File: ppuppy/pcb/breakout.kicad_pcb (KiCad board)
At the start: 2 copper layers, 48 parts, among them Q1 2N3904, Q2 2N3904, Q3 2N3904, Q4 2N3904, Q5 2N3904, Q6 2N3904, Q7 2N3904, Q8 2N3904

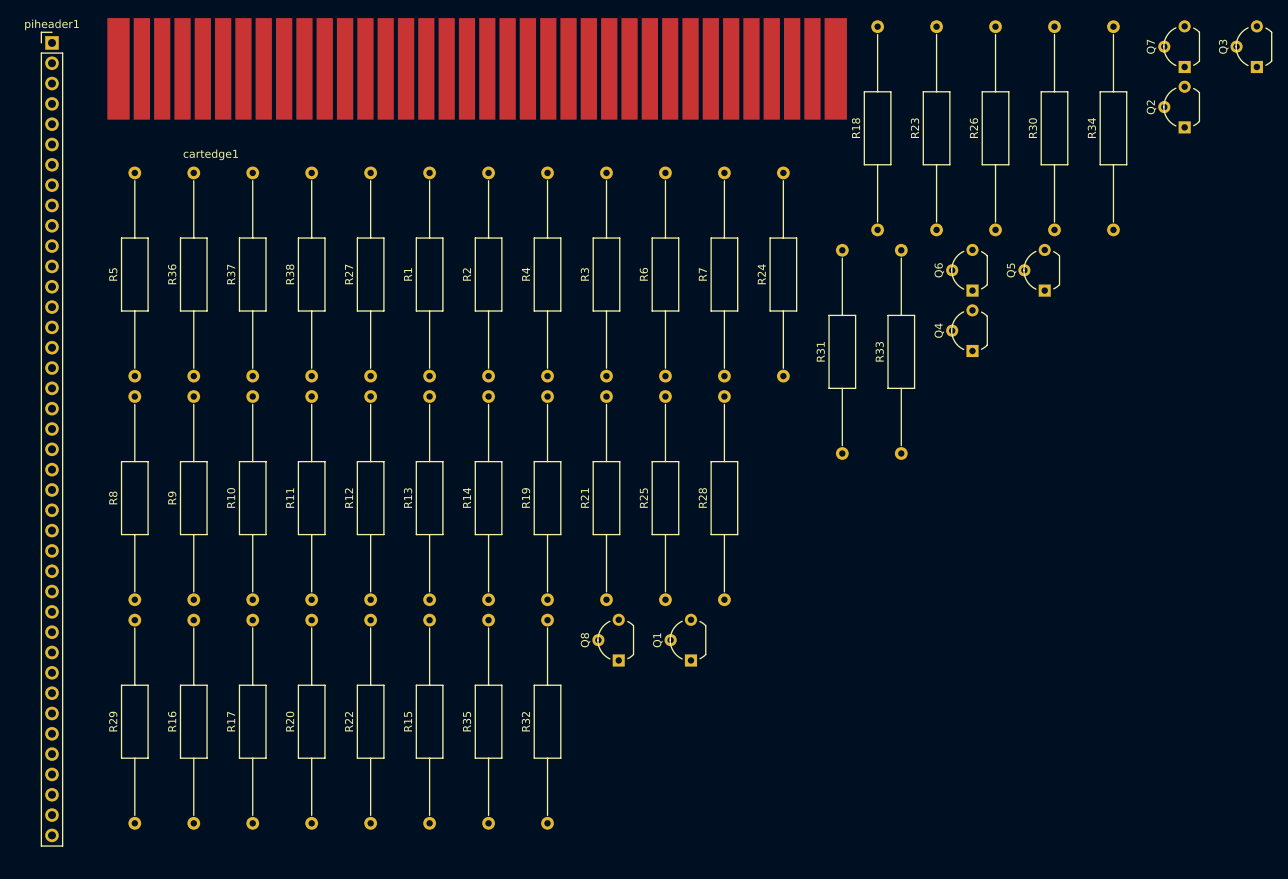
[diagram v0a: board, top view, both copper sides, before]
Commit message: new breakout with eeprom and headers
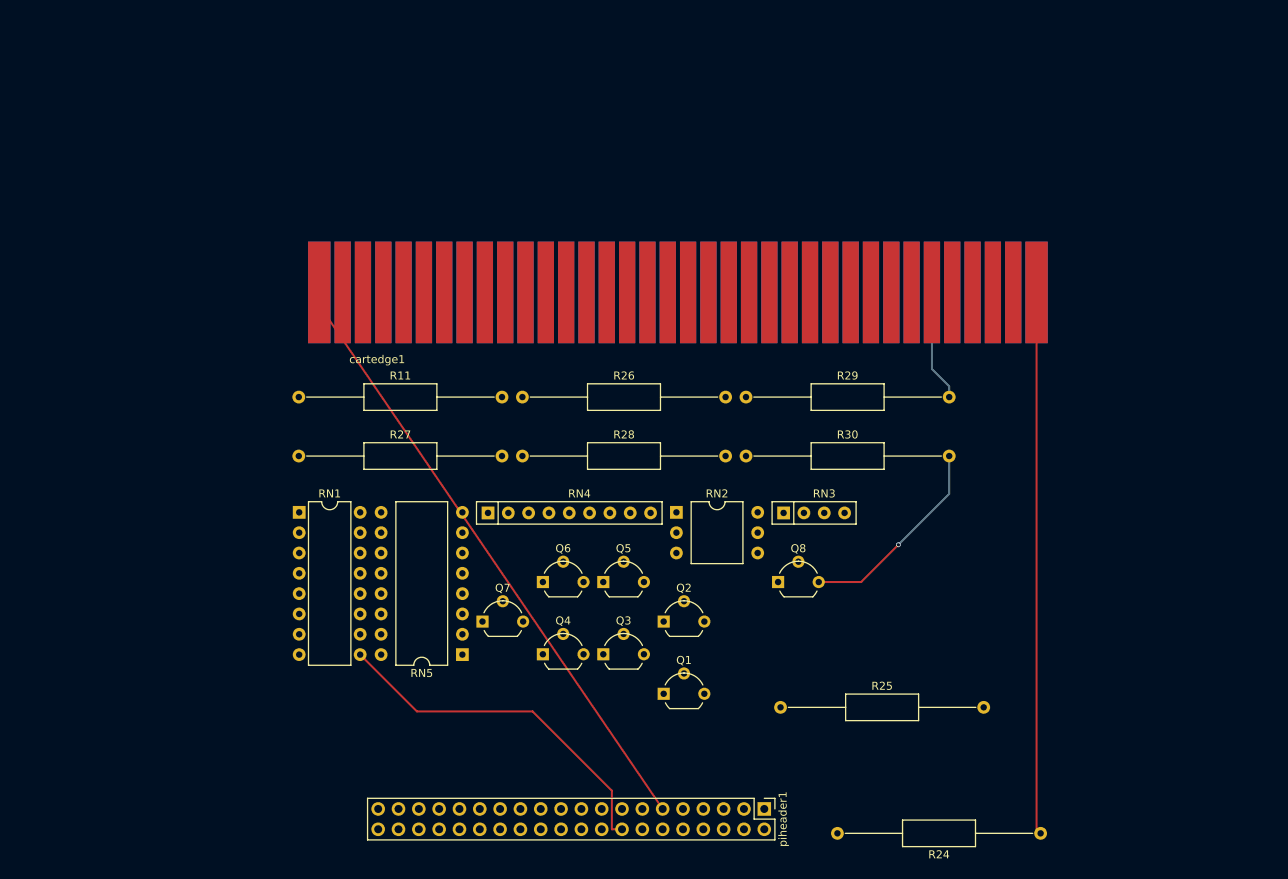
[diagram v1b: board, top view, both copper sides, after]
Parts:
- removed R1, R10, R12, R14, R17, R18, R20, R22, R4, R5, R7: 2k, Resistors_THT:R_Axial_DIN0309_L9.0mm_D3.2mm_P25.40mm_Horizontal
- removed R13, R15, R16, R19, R2, R21, R23, R3, R6, R8, R9: 1k, Resistors_THT:R_Axial_DIN0309_L9.0mm_D3.2mm_P25.40mm_Horizontal
- removed R31, R32, R33, R34, R35, R36, R37, R38: 10k, Resistors_THT:R_Axial_DIN0309_L9.0mm_D3.2mm_P25.40mm_Horizontal
- added RN1: 10k, Housings_DIP:DIP-16_W7.62mm, F.Cu at (90.5, 94.8)
- added RN2: 1k, Housings_DIP:DIP-6_W10.16mm, F.Cu at (137.6, 94.8)
- added RN3: 2k, Resistors_THT:R_Array_SIP4, F.Cu at (151.0, 94.8)
- added RN4: 2k, Resistors_THT:R_Array_SIP9, F.Cu at (114.1, 94.8)
- added RN5: 1k, Housings_DIP:DIP-16_W10.16mm, F.Cu at (110.9, 112.5)
- piheader1: footprint Pin_Headers:Pin_Header_Straight_1x40_Pitch2.54mm -> Pin_Headers:Pin_Header_Straight_2x20_Pitch2.54mm
- moved piheader1 130.8 mm to (148.6, 131.8), turned to 270 degrees
- moved Q7 111.8 mm to (113.4, 108.4), turned to 0 degrees
- moved Q3 109.8 mm to (128.5, 112.5), turned to 0 degrees
- moved R29 93.1 mm to (146.3, 80.3), turned to 0 degrees
- moved Q2 89.8 mm to (136.0, 108.4), turned to 0 degrees
- moved Q5 66.1 mm to (128.5, 103.5), turned to 0 degrees
- moved Q4 65.7 mm to (120.9, 112.5), turned to 0 degrees
- moved R24 65.6 mm to (183.1, 134.9), turned to 180 degrees
- moved Q6 64.9 mm to (120.9, 103.5), turned to 0 degrees
- moved R26 62.7 mm to (118.4, 80.3), turned to 0 degrees
- moved R30 47.8 mm to (146.3, 87.7), turned to 0 degrees
- moved R28 31.0 mm to (118.4, 87.7), turned to 0 degrees
- moved cartedge1 26.9 mm to (91.3, 73.6)
- moved R11 25.4 mm to (90.4, 80.3), turned to 0 degrees
- moved Q8 22.2 mm to (150.3, 103.5), turned to 0 degrees
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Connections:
- cartedge1 pad 10: Net-(cartedge1-Pad10) -> (no net)
- cartedge1 pad 11: Net-(cartedge1-Pad11) -> (no net)
- cartedge1 pad 12: Net-(cartedge1-Pad12) -> (no net)
- cartedge1 pad 13: Net-(cartedge1-Pad13) -> (no net)
- cartedge1 pad 14: Net-(cartedge1-Pad14) -> (no net)
- cartedge1 pad 15: Net-(cartedge1-Pad15) -> (no net)
- cartedge1 pad 16: Net-(cartedge1-Pad16) -> (no net)
- cartedge1 pad 17: Net-(cartedge1-Pad17) -> (no net)
- cartedge1 pad 18: Net-(cartedge1-Pad18) -> (no net)
- cartedge1 pad 19: Net-(cartedge1-Pad19) -> (no net)
- cartedge1 pad 2: Net-(cartedge1-Pad2) -> (no net)
- cartedge1 pad 20: Net-(cartedge1-Pad20) -> (no net)
- cartedge1 pad 22: Net-(cartedge1-Pad22) -> (no net)
- cartedge1 pad 3: Net-(cartedge1-Pad3) -> (no net)
- cartedge1 pad 34: Net-(cartedge1-Pad34) -> (no net)
- cartedge1 pad 35: Net-(cartedge1-Pad35) -> (no net)
- cartedge1 pad 4: Net-(cartedge1-Pad4) -> (no net)
- cartedge1 pad 5: Net-(cartedge1-Pad5) -> (no net)
- cartedge1 pad 6: Net-(cartedge1-Pad6) -> (no net)
- cartedge1 pad 7: Net-(cartedge1-Pad7) -> (no net)
- cartedge1 pad 8: Net-(cartedge1-Pad8) -> (no net)
- cartedge1 pad 9: Net-(cartedge1-Pad9) -> (no net)
- piheader1 pad 1: Net-(piheader1-Pad1) -> (no net)
- piheader1 pad 10: Net-(piheader1-Pad10) -> (no net)
- piheader1 pad 14: Net-(piheader1-Pad14) -> (no net)
- piheader1 pad 17: Net-(piheader1-Pad17) -> (no net)
- piheader1 pad 19: Net-(piheader1-Pad19) -> (no net)
- piheader1 pad 20: Net-(piheader1-Pad20) -> (no net)
- piheader1 pad 21: Net-(piheader1-Pad21) -> (no net)
- piheader1 pad 23: Net-(piheader1-Pad23) -> (no net)
- piheader1 pad 25: Net-(piheader1-Pad25) -> (no net)
- piheader1 pad 27: Net-(piheader1-Pad27) -> (no net)
- piheader1 pad 28: Net-(piheader1-Pad28) -> (no net)
- piheader1 pad 30: Net-(piheader1-Pad30) -> (no net)
- piheader1 pad 32: Net-(piheader1-Pad32) -> (no net)
- piheader1 pad 33: Net-(piheader1-Pad33) -> (no net)
- piheader1 pad 34: Net-(piheader1-Pad34) -> (no net)
- piheader1 pad 39: Net-(piheader1-Pad39) -> (no net)
- piheader1 pad 4: Net-(piheader1-Pad4) -> (no net)
- piheader1 pad 8: Net-(piheader1-Pad8) -> (no net)
- piheader1 pad 9: Net-(piheader1-Pad9) -> (no net)
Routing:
- net GND: track 0.00 -> 79.2 mm
- net 5V: track 0.00 -> 67.8 mm
- net Net-(RN1-Pad9): track 0.00 -> 44.6 mm
- net Net-(Q8-Pad3): track 0.00 -> 25.6 mm, vias 0 -> 1
- net Net-(Q7-Pad3): track 0.00 -> 14.0 mm
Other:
- rule pad_to_mask_clearance: 0.2 -> 0
